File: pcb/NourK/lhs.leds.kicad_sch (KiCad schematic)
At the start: 43 parts

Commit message: Draft LHS tracks
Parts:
- removed C? (x3): 0.1uF, Capacitor_SMD:C_0805_2012Metric, symbol Device:C
- removed C? (x4): 0.47uF, Capacitor_SMD:C_0805_2012Metric, symbol Device:C
- removed IC?: IS31FL3733B-QFLS4-TR, Nour_KB:QFN40P600X600X80-49N-D, symbol Nour_KB:IS31FL3733B-QFLS4-TR
- removed R? (x2): R, Resistor_SMD:R_0805_2012Metric, symbol Device:R
- gave numbers to parts that had none: 33
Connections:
- net BL_LED_COL1 renamed LED.CS_COL1
- net BL_LED_COL2 renamed LED.CS_COL2
- net BL_LED_COL3 renamed LED.CS_COL3
- net BL_LED_COL4 renamed LED.CS_COL4
- net BL_LED_COL5 renamed LED.CS_COL5
- net BL_LED_COL6 renamed LED.CS_COL6
- net BL_LED_COL7 renamed LED.CS_COL7
- net LED_BLUE_ROW1 renamed LED.SW_BLUE1
- net LED.SW_BLUE1: now also D79.3 (BK), D81.3 (BK); no longer D75.3 (BK)
- net LED_BLUE_ROW2 renamed LED.SW_BLUE2
- net LED.SW_BLUE2: now also D75.3 (BK), D82.3 (BK); no longer D76.3 (BK), D79.3 (BK)
- net LED_BLUE_ROW3 renamed LED.SW_BLUE3
- net LED.SW_BLUE3: now also D80.3 (BK); no longer D78.3 (BK), D81.3 (BK)
- net LED_BLUE_ROW4 renamed LED.SW_BLUE4
- net LED.SW_BLUE4: now also D76.3 (BK), D78.3 (BK); no longer D80.3 (BK), D82.3 (BK)
- net LED_GREEN_ROW1 renamed LED.SW_GREEN1
- net LED.SW_GREEN1: now also D79.4 (GK), D81.4 (GK); no longer D75.4 (GK)
- net LED_GREEN_ROW2 renamed LED.SW_GREEN2
- net LED.SW_GREEN2: now also D75.4 (GK), D82.4 (GK); no longer D76.4 (GK), D79.4 (GK)
- net LED_GREEN_ROW3 renamed LED.SW_GREEN3
- net LED.SW_GREEN3: now also D80.4 (GK); no longer D78.4 (GK), D81.4 (GK)
- net LED_GREEN_ROW4 renamed LED.SW_GREEN4
- net LED.SW_GREEN4: now also D76.4 (GK), D78.4 (GK); no longer D80.4 (GK), D82.4 (GK)
- net LED_RED_ROW1 renamed LED.SW_RED1
- net LED.SW_RED1: now also D79.2 (RK), D81.2 (RK); no longer D75.2 (RK)
- net LED_RED_ROW2 renamed LED.SW_RED2
- net LED.SW_RED2: now also D75.2 (RK), D82.2 (RK); no longer D76.2 (RK), D79.2 (RK)
- net LED_RED_ROW3 renamed LED.SW_RED3
- net LED.SW_RED3: now also D80.2 (RK); no longer D78.2 (RK), D81.2 (RK)
- net LED_RED_ROW4 renamed LED.SW_RED4
- net LED.SW_RED4: now also D76.2 (RK), D78.2 (RK); no longer D80.2 (RK), D82.2 (RK)
- net UG_LED_COL1 renamed LED.CS_COL11
- net LED.CS_COL11: no longer D77.1 (A), D79.1 (A)
- net UG_LED_COL2 renamed LED.CS_COL8
- net LED.CS_COL8: now also D77.1 (A); no longer D78.1 (A), D80.1 (A)
- new net LED.CS_COL10: D79.1 (A), D80.1 (A)
- new net LED.CS_COL9: D78.1 (A)
- no-connect marks 11 -> 0
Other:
- note removed: "Chip shutdown"
- note removed: "I2C ADDR 1010000x"
- note removed: "LEDs current source value"
- note removed: "Reset Switch"
- note removed: "TODO: - Check LED pins after choosing LEDs. - LEDs must be same current."
- note removed: "VDD 2.7V to 5.5V"
- moved on the sheet: D50, D51, D52, D53, D54, D55, D56, D57, D58, D59, D60, D61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

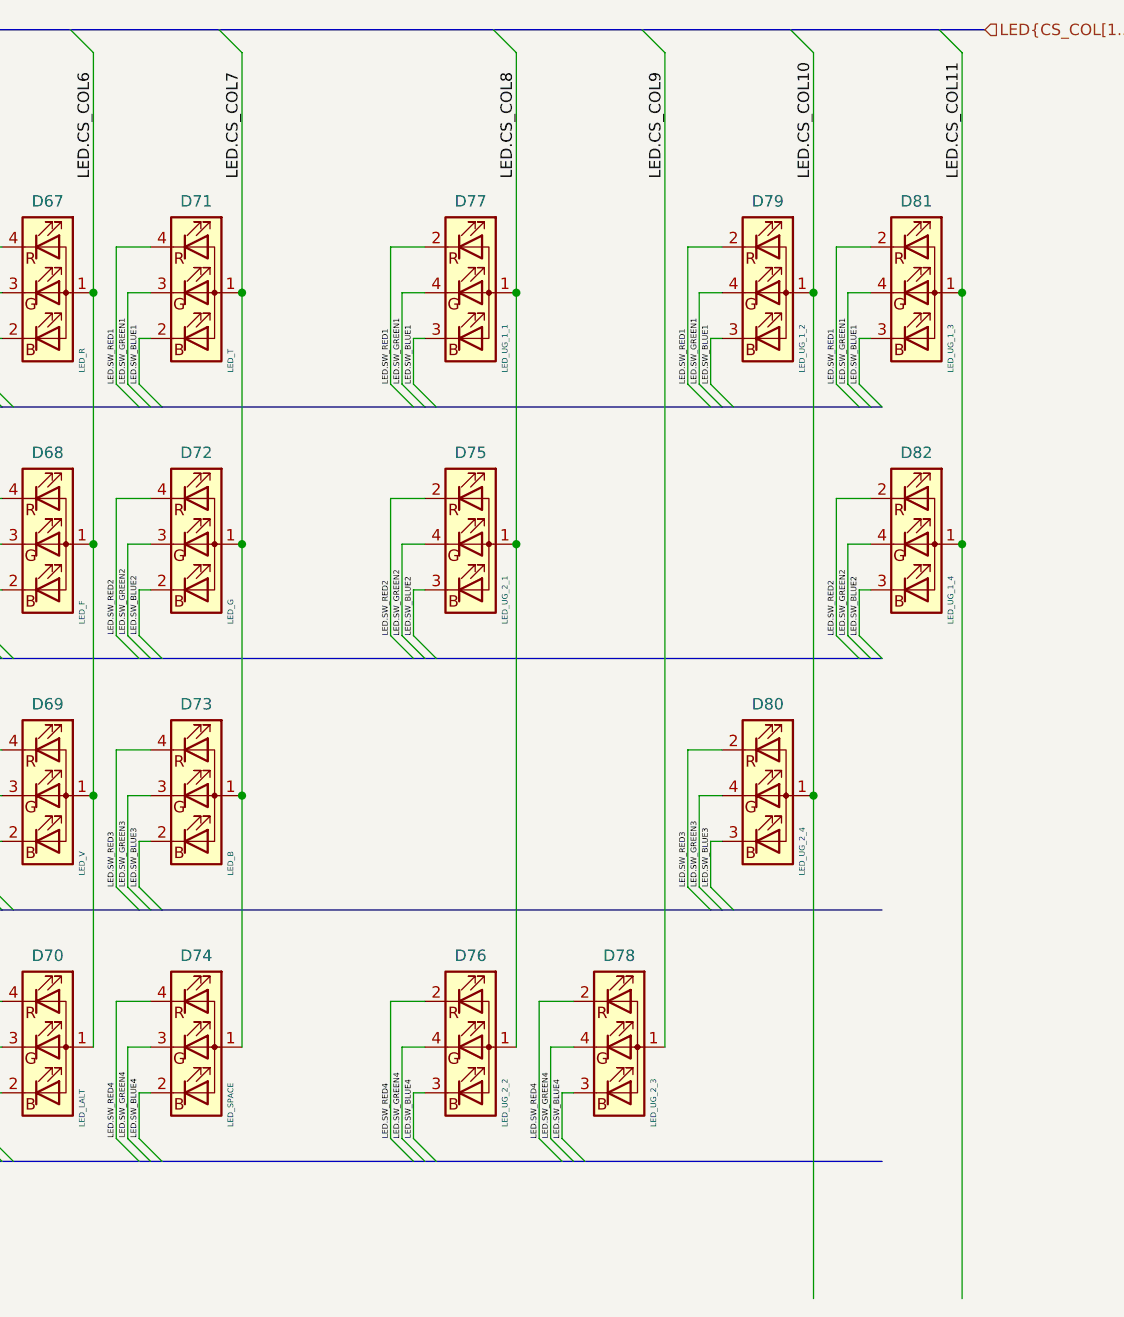
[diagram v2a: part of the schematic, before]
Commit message: RHS and LHS wire complete and initial DRC
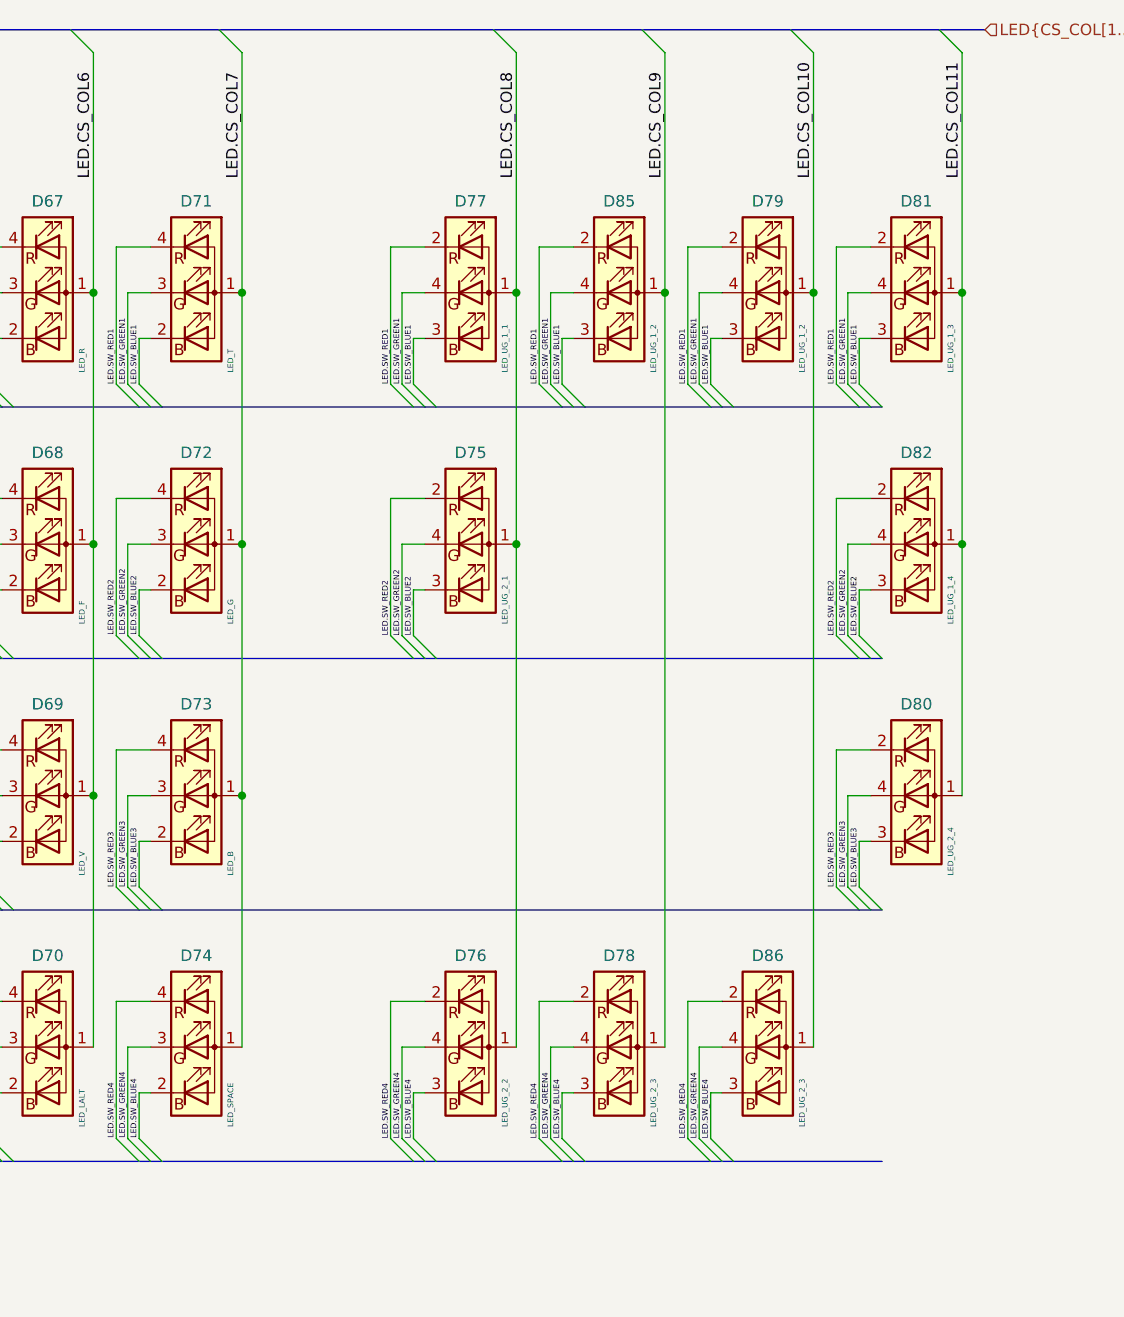
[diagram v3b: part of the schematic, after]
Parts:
- added D85: LED_UG_1_2, Nour_KB:LTRBR37G4R4S012502R18, symbol Device:LED_ARBG
- added D86: LED_UG_2_3, Nour_KB:LTRBR37G4R4S012502R18, symbol Device:LED_ARBG
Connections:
- net LED.CS_COL10: now also D86.1 (A); no longer D80.1 (A)
- net LED.CS_COL11: now also D80.1 (A)
- net LED.CS_COL9: now also D85.1 (A)
- net LED.SW_BLUE1: now also D85.3 (BK)
- net LED.SW_BLUE4: now also D86.3 (BK)
- net LED.SW_GREEN1: now also D85.4 (GK)
- net LED.SW_GREEN4: now also D86.4 (GK)
- net LED.SW_RED1: now also D85.2 (RK)
- net LED.SW_RED4: now also D86.2 (RK)
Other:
- moved on the sheet: D80
